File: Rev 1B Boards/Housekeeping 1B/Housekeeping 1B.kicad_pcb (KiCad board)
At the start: 2 copper layers, 48 parts, among them J15 Banana 2P, J21 Banana 2P, J22 Banana 2P, J24 Banana 2P, U1 MC34063A, U2 MC34063A, U3 TPS54302

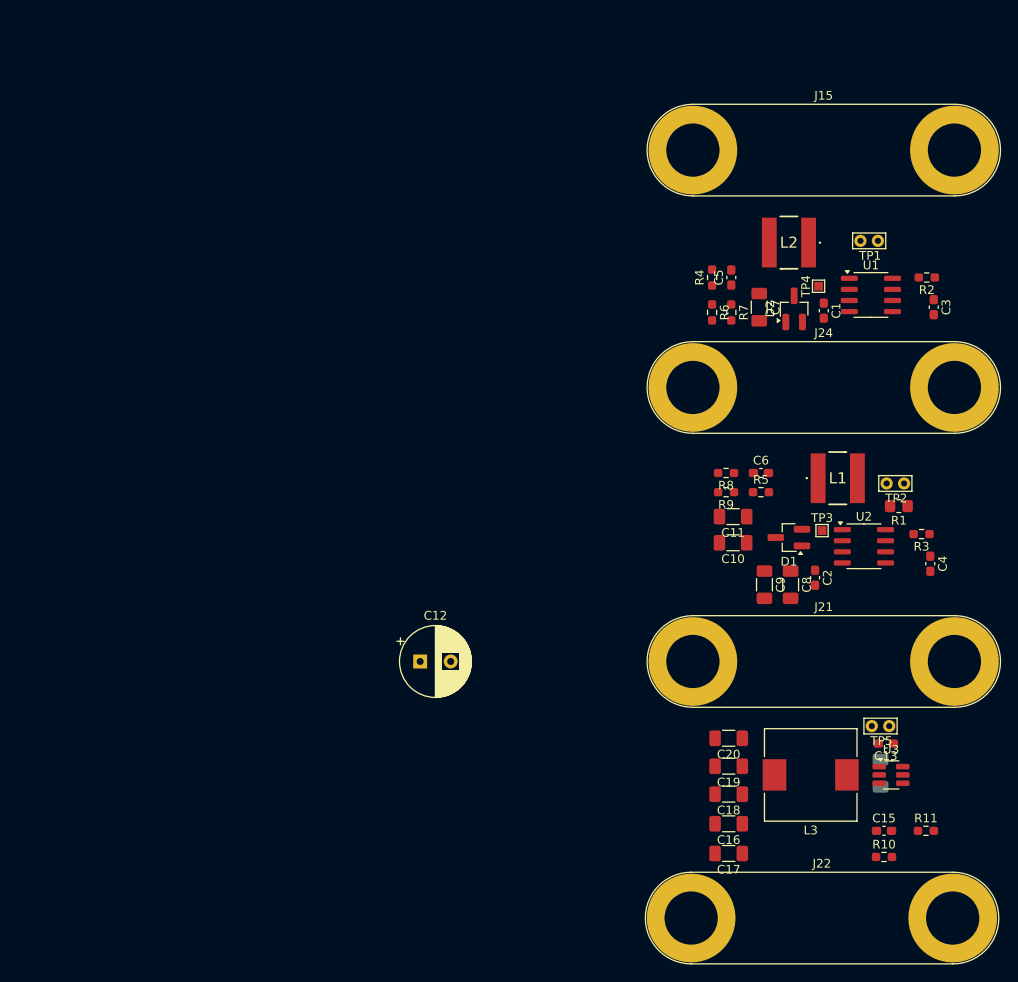
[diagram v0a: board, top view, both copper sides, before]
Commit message: Completed layout of housekeeping supplies
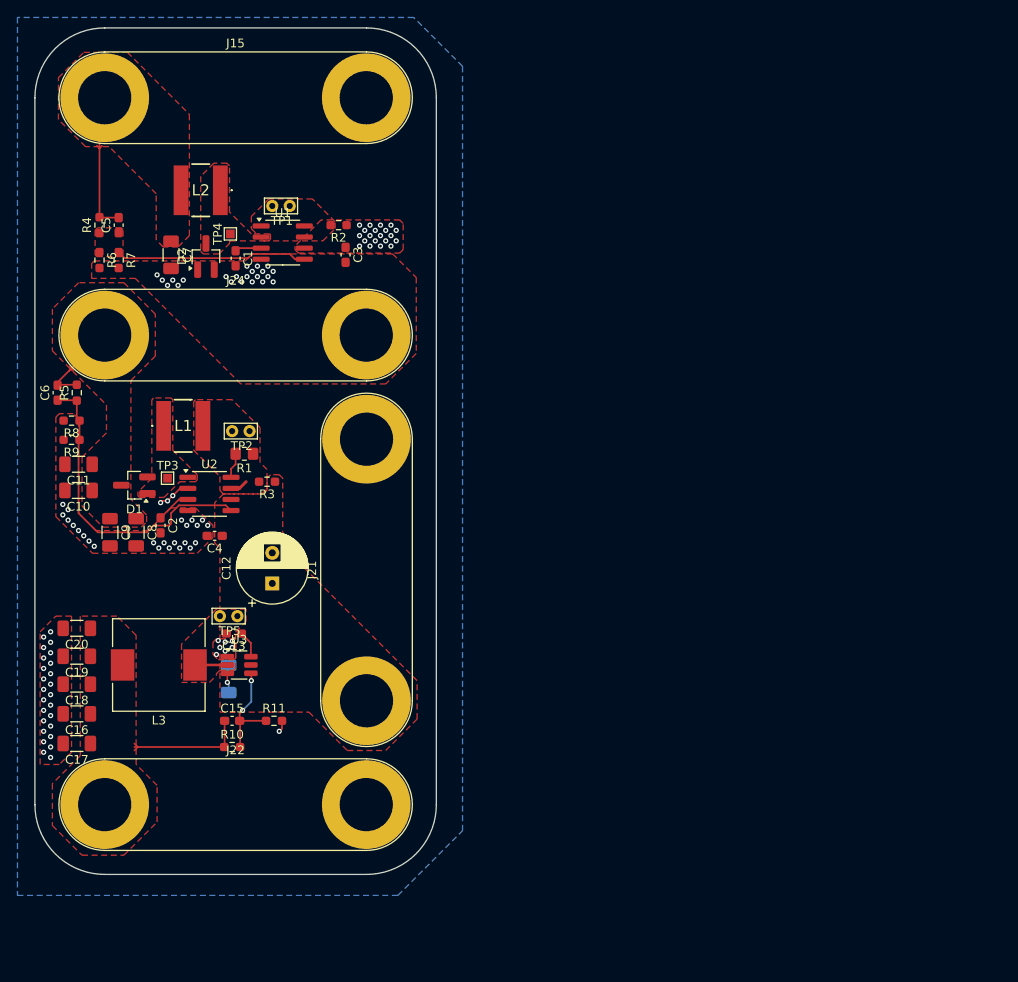
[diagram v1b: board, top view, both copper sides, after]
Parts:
- moved C4 82.1 mm to (157.2, 83.6), turned to 180 degrees
- moved C6 81.1 mm to (139.2, 67.2), turned to 90 degrees
- moved R5 79.2 mm to (141.4, 67.2), turned to 90 degrees
- moved C15 75.8 mm to (159.2, 104.8)
- moved R10 75.8 mm to (159.2, 107.8)
- moved C13 75.8 mm to (159.4, 94.8)
- moved C16 75.8 mm to (141.4, 104.0)
- moved C17 75.8 mm to (141.4, 107.4)
- moved C18 75.8 mm to (141.4, 100.6)
- moved C19 75.8 mm to (141.4, 97.4)
- moved C20 75.8 mm to (141.4, 94.2)
- moved L3 75.8 mm to (150.8, 98.4)
- moved R11 75.8 mm to (164.0, 104.8)
- moved TP5 75.8 mm to (157.8, 92.8)
- moved U3 75.8 mm to (160.0, 98.4)
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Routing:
- net /Housekeeping Power Supplies/30V_COMP: track 0.00 -> 35.9 mm
- net /Housekeeping Power Supplies/3V3_COMP: track 0.00 -> 22.0 mm
- net +3V3: track 0.00 -> 17.0 mm
- net +5V: track 0.00 -> 14.4 mm
- net /Housekeeping Power Supplies/FB: track 0.00 -> 12.1 mm, vias 0 -> 2
- net VCC: track 0.00 -> 11.1 mm
- net GND: track 0.00 -> 5.43 mm, vias 0 -> 60
- net /Housekeeping Power Supplies/30V_CT: track 0.00 -> 4.00 mm
- net /Housekeeping Power Supplies/SW: track 0.00 -> 3.70 mm
- net /Housekeeping Power Supplies/BOOT: track 0.00 -> 3.10 mm
- net /Housekeeping Power Supplies/3V3_CT: track 0.00 -> 3.05 mm
- net /Housekeeping Power Supplies/30V_DC: track 0.00 -> 2.91 mm
- net /+24_{MiniPC}: track 0.00 -> 2.27 mm, vias 0 -> 43
- net /Housekeeping Power Supplies/30V_VC: track 0.00 -> 2.04 mm
- added copper zone on F.Cu, net +3V3
- added copper zone on F.Cu, net +5V
- added copper zone on F.Cu, net /+24_{MiniPC}
- added copper zone on In2.Cu, net /+24_{MiniPC}
- added copper zone on F.Cu, net /Housekeeping Power Supplies/30V_SW
- added copper zone on F.Cu, net /Housekeeping Power Supplies/30V_VC
- added copper zone on F.Cu, net /Housekeeping Power Supplies/3V3_COMP
- added copper zone on F.Cu, net /Housekeeping Power Supplies/3V3_SW
- added copper zone on F.Cu, net /Housekeeping Power Supplies/3V3_VC
- added copper zone on F.Cu, net /Housekeeping Power Supplies/SW
- added copper zone on B.Cu, net GND
- added copper zone on F.Cu, net GND
- added copper zone on In1.Cu, net GND
- added copper zone on F.Cu, net VCC
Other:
- board outline added: 46 x 97 mm
- copper layers 2 -> 4

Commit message: Fix DRC issues
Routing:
- net /+24_{MiniPC}: vias 43 -> 21
- net GND: vias 60 -> 82

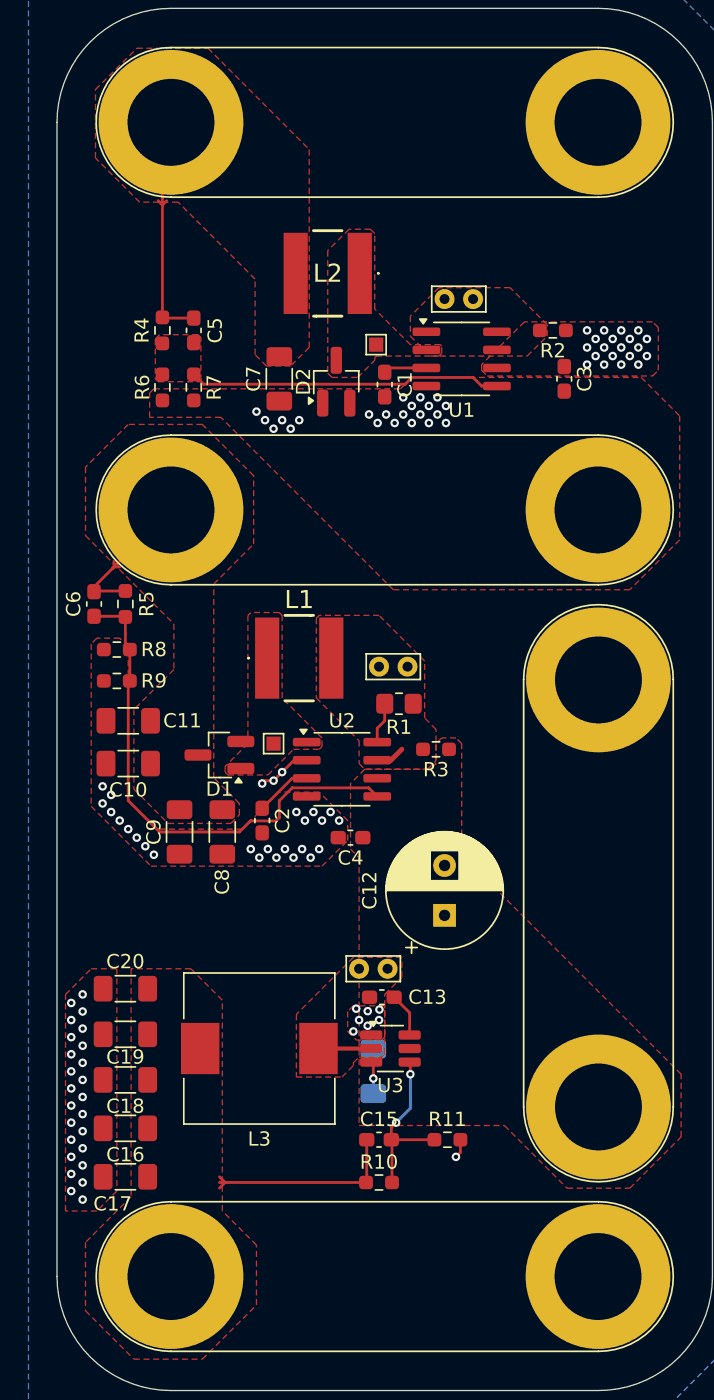
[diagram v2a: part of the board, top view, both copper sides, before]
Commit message: Completed Housekeeping layout
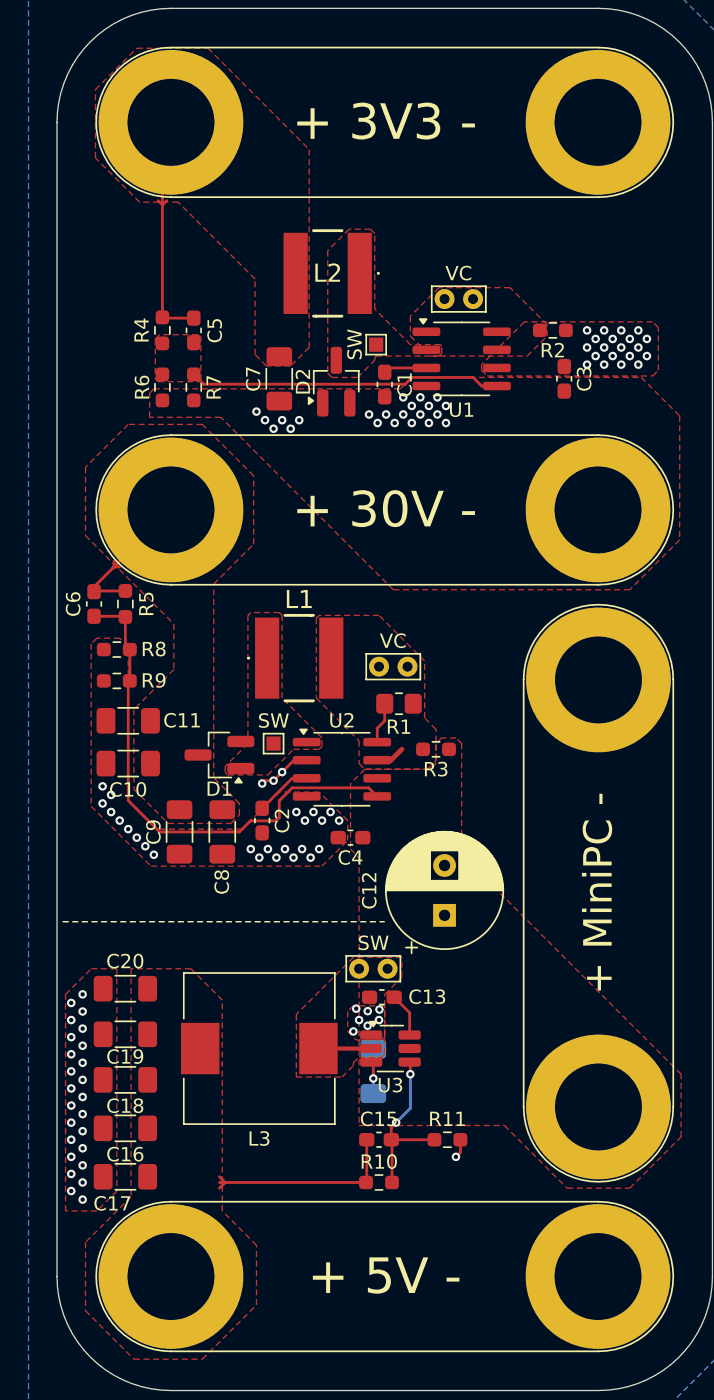
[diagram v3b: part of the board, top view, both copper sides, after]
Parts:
- added G***: LOGO, ! Robomaster Special:StampedeLogo, B.Cu at (159.6, 33.4)
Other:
- board text added: "+ 30V -"
- board text added: "+ 3V3 -"
- board text added: "+ 5V -"
- board text added: "+ MiniPC -"
- board text added: "SW"
- board text added: "UT Stampede Supercap Housekeeping Power Supplies Test Board _{Egan Wang, Jed Wang}"
- board text added: "VC"

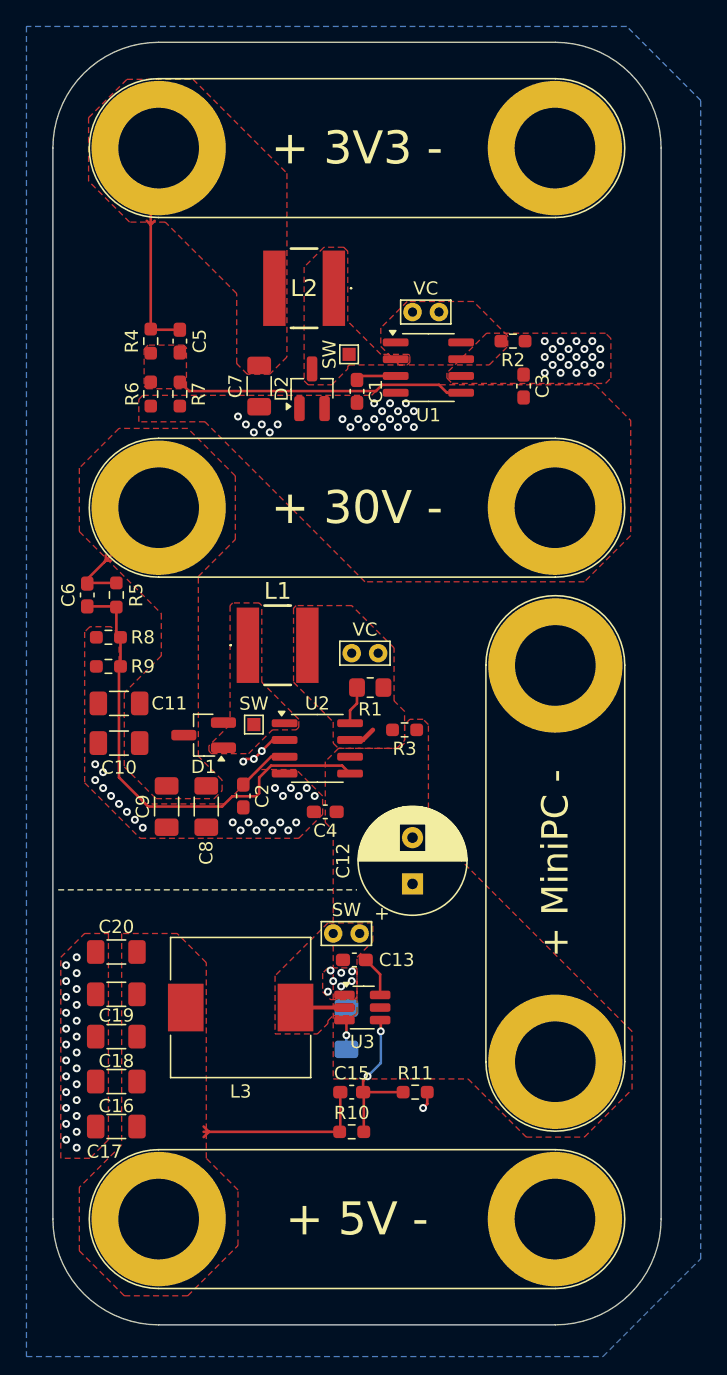
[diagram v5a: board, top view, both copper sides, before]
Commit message: Replace most banana jacks with XT connectors
+ update library
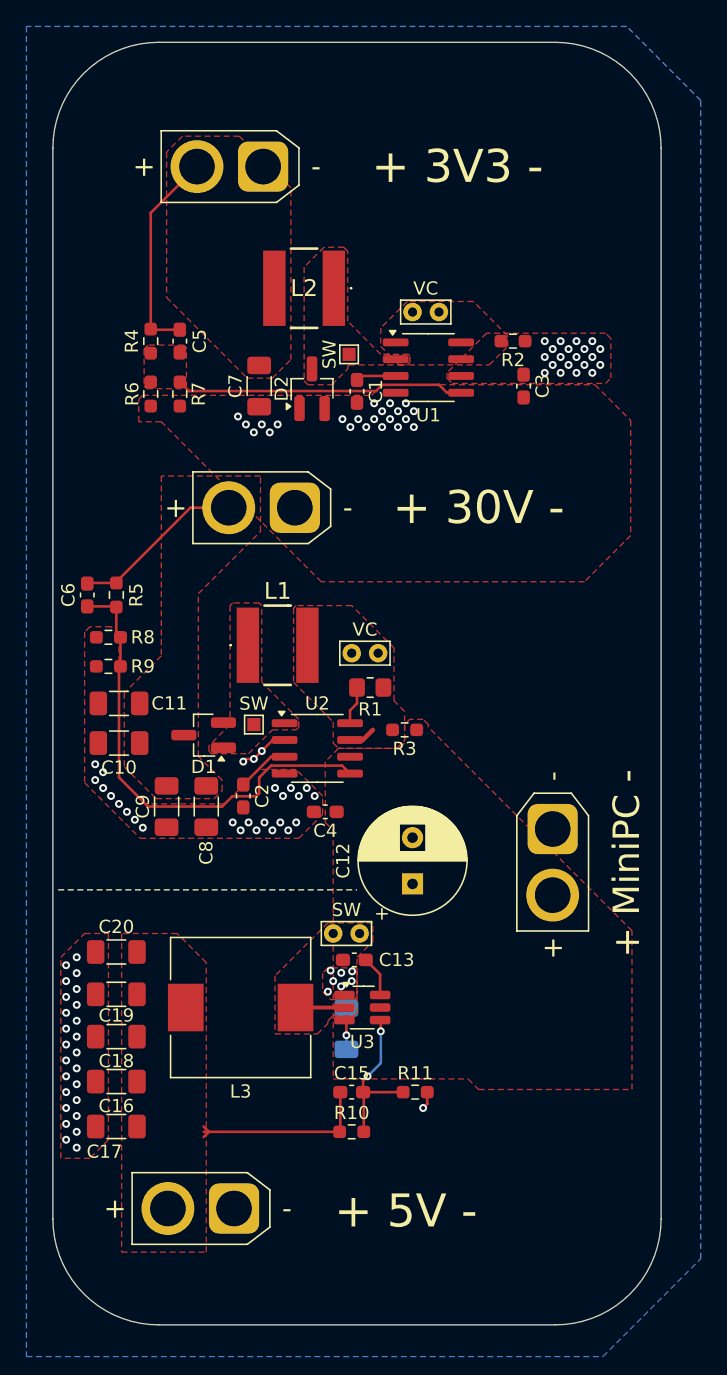
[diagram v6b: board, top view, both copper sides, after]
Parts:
- removed J21, J22, J24: Banana 2P, Connector:Banana_Jack_2Pin
- added J14: XT30_F, Connector_AMASS:AMASS_XT30U-F_1x02_P5.0mm_Vertical, F.Cu at (174.4, 84.9)
- added J16: XT30_F, Connector_AMASS:AMASS_XT30U-F_1x02_P5.0mm_Vertical, F.Cu at (150.3, 113.6)
- added J17: XT30_F, Connector_AMASS:AMASS_XT30U-F_1x02_P5.0mm_Vertical, F.Cu at (152.5, 34.8)
- J15: value Banana 2P -> XT30_F; footprint Connector:Banana_Jack_2Pin -> Connector_AMASS:AMASS_XT30U-F_1x02_P5.0mm_Vertical
- moved J15 29.1 mm to (154.9, 60.6), turned to 180 degrees
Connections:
- J15 pad 1: +3V3 -> GND
- J15 pad 2: GND -> VCC
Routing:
- net VCC: track 11.1 -> 13.5 mm
- net +3V3: track 17.0 -> 16.0 mm
